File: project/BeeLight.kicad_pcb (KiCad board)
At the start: 2 copper layers, 32 x 24 mm, 25 parts, among them IC101 BT40F, IC102 APDS-9306-065, IC103 BME688, Q101 BSS84, SW101 JOIN, X102 DEBUG

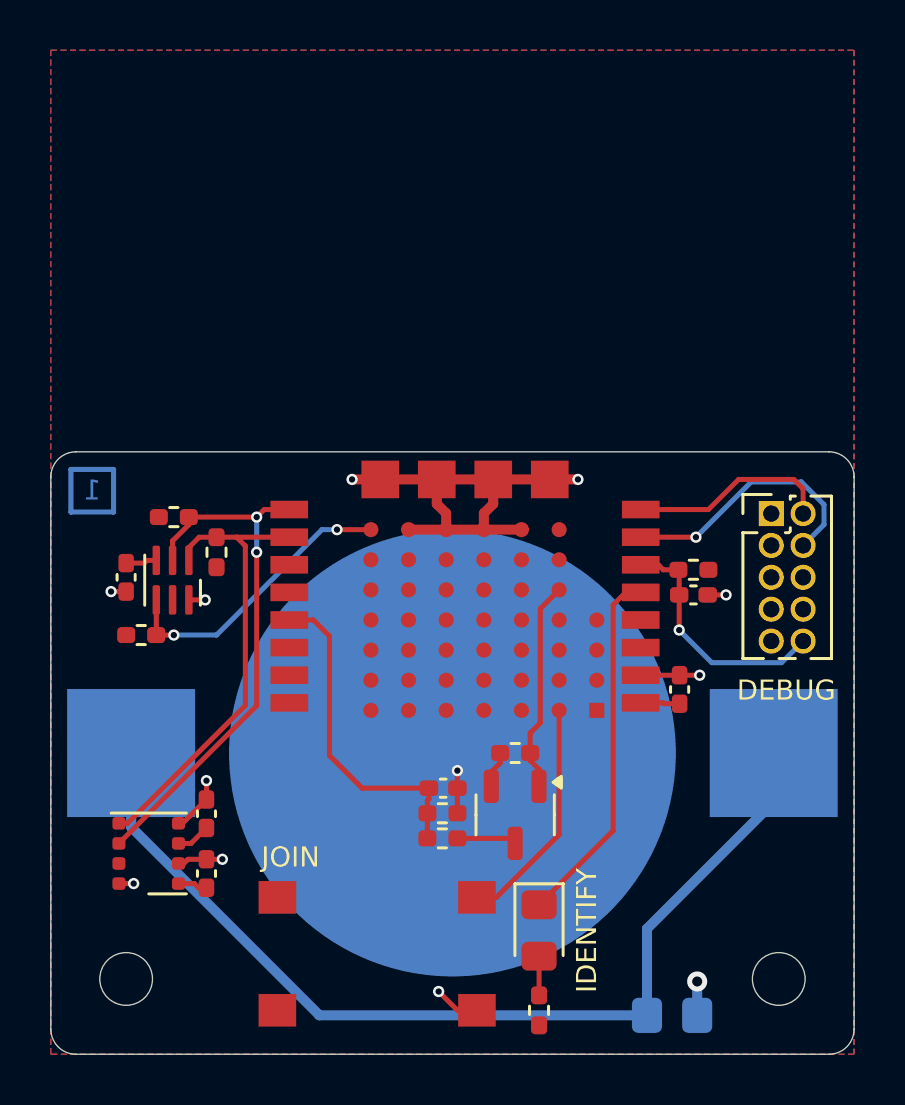
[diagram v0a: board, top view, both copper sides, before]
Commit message: Replace nRF53 with nRF54L
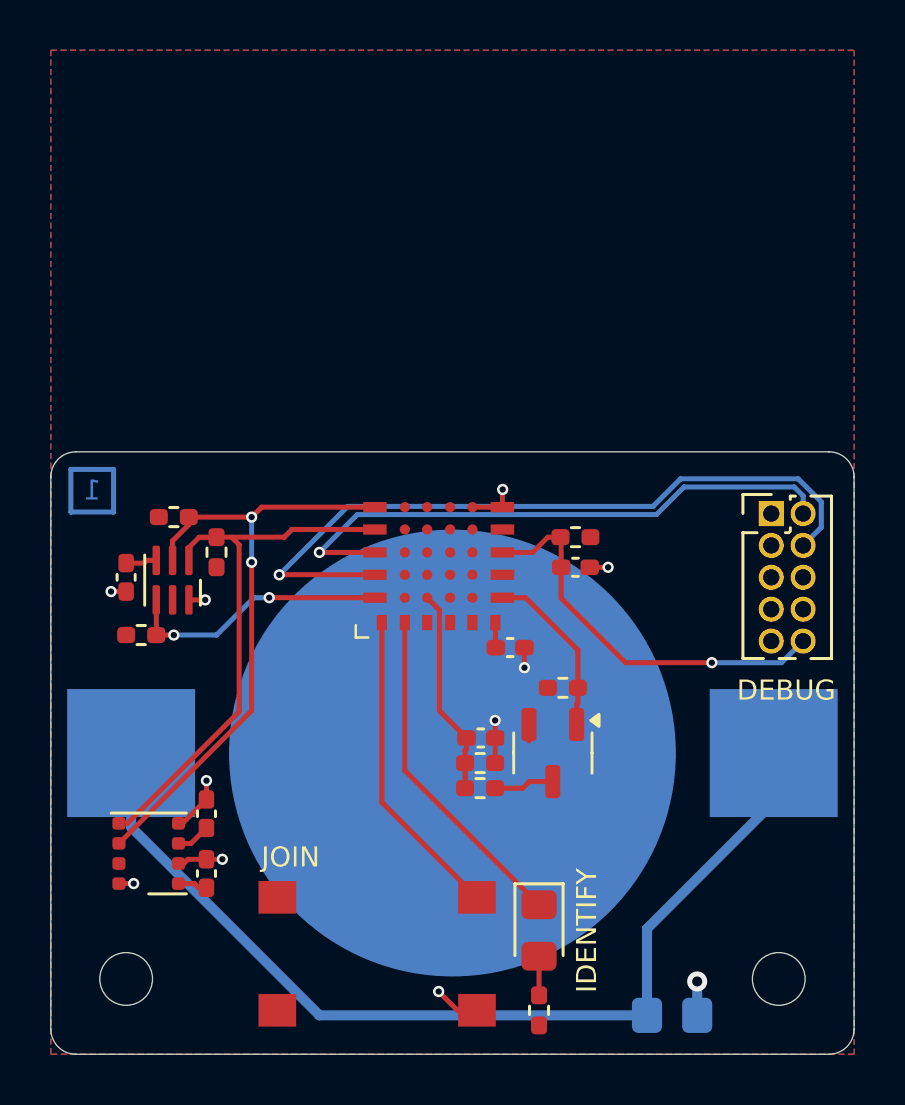
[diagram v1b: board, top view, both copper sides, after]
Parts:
- removed IC101: BT40F, Fanstel:XCVR_BT40F
- added M101: BC15C, Fanstel:BC15C, F.Cu at (138.0, 83.0)
- moved C102 6.95 mm to (140.3, 89.8), turned to 0 degrees
- moved R101 4.88 mm to (142.9, 85.4)
- moved C101 4.83 mm to (142.9, 86.6)
- moved R107 3.22 mm to (142.4, 91.4)
- moved Q101 2.88 mm to (142.0, 94.0)
- moved C103 2.50 mm to (139.1, 93.4)
- moved R108 2.50 mm to (139.1, 95.4)
- moved R109 2.50 mm to (139.1, 94.4)
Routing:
- net SWDCLK: track 10.6 -> 29.4 mm
- net GND: track 30.5 -> 12.9 mm, vias 11 -> 10
- net SWDIO: track 8.11 -> 23.4 mm, vias 0 -> 1
- net ~{RESET}: track 9.79 -> 16.1 mm
- net V_{BAT}: track 13.2 -> 8.27 mm
- net SCL: track 18.5 -> 21.9 mm
- net SDA: track 21.4 -> 24.8 mm
- net Net-(M101-P2.05): track 9.26 -> 12.5 mm
- net BAT_E: track 8.65 -> 6.86 mm
- net +BATT: track 8.38 -> 6.93 mm
- net INT: track 11.7 -> 10.7 mm
- net Net-(D101-K): track 14.3 -> 13.5 mm
